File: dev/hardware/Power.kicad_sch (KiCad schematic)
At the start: 5 parts, among them U2 LD1117V33

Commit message: Continued developing JCAP schematic
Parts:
- D301: value LED -> POWER LED
- R301: value R -> 100
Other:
- moved on the sheet: C2, D301, R301, U2

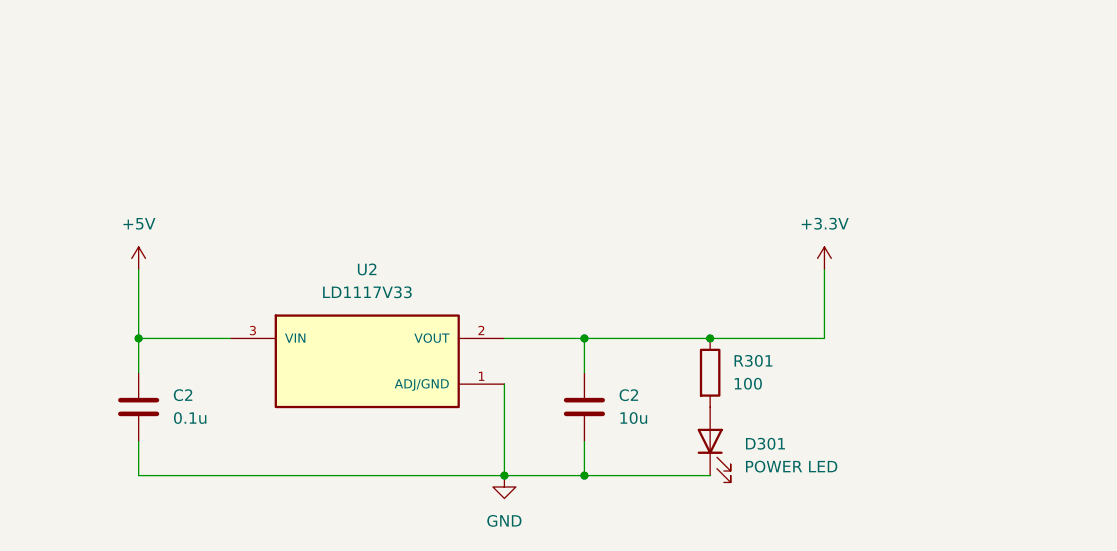
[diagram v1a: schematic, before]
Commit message: Finalized initial schematic
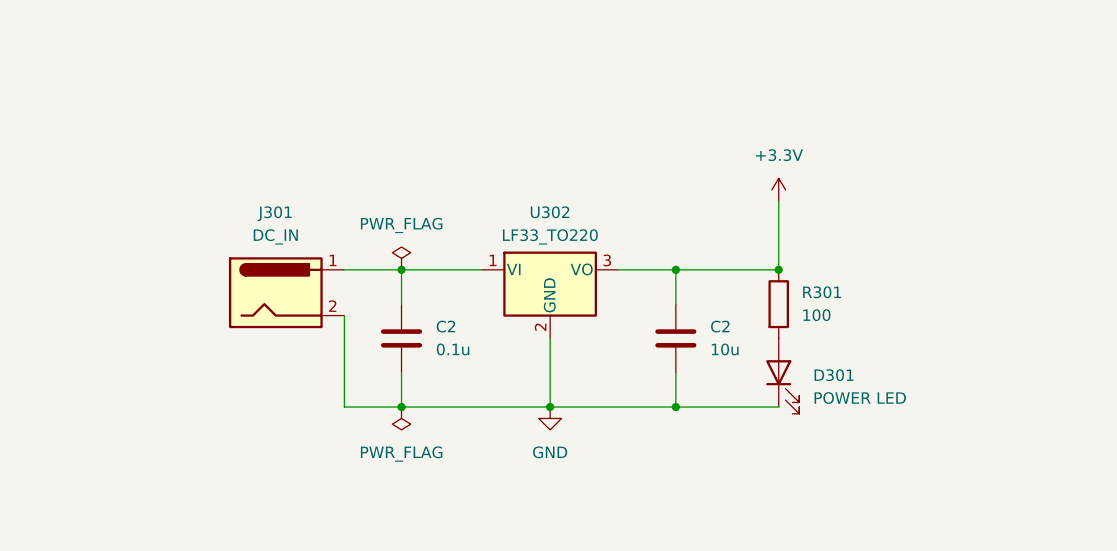
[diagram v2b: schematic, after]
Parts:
- removed U2: LD1117V33, jcap_footprint_library:TO255P1020X450X1968-3, symbol jcap_symbol_library:LD1117V33
- added J301: DC_IN, Connector_BarrelJack:BarrelJack_CUI_PJ-063AH_Horizontal_CircularHoles, symbol Connector:Barrel_Jack
- added U302: LF33_TO220, Package_TO_SOT_THT:TO-220-3_Vertical, symbol Regulator_Linear:LF33_TO220
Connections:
- net +3.3V: now also U302.3 (VO)
- net GND: now also J301.2, U302.2 (GND)
- net +5V: no longer names the net of C2.1
- net +5V: now also J301.1, U302.1 (VI)
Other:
- moved on the sheet: C2, D301, R301

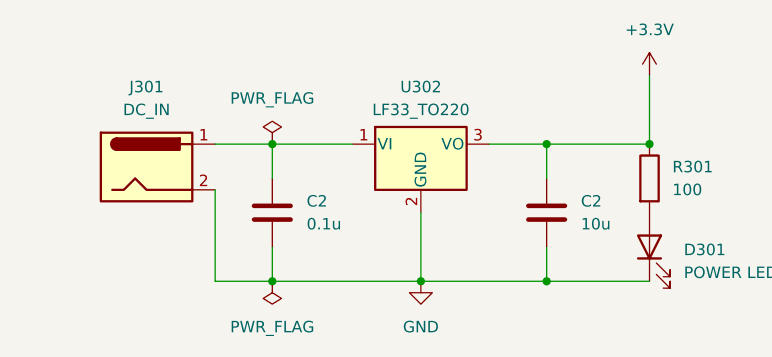
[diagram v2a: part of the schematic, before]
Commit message: Started developing PCB layout
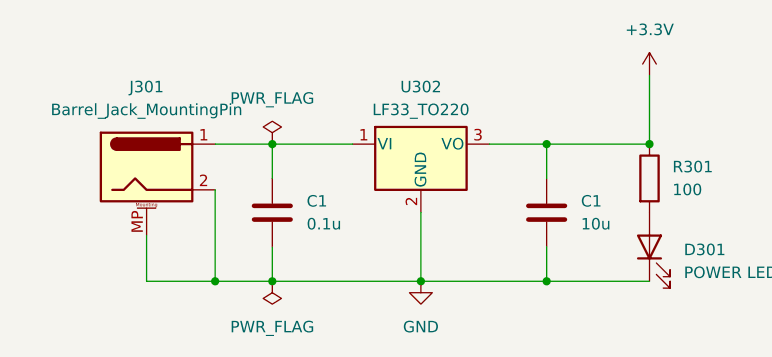
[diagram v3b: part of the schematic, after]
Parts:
- removed C2: 10u, Capacitor_THT:C_Radial_D4.0mm_H7.0mm_P1.50mm, symbol Device:C
- removed C2: 0.1u, Capacitor_THT:C_Radial_D4.0mm_H7.0mm_P1.50mm, symbol Device:C
- removed J301: DC_IN, Connector_BarrelJack:BarrelJack_CUI_PJ-063AH_Horizontal_CircularHoles, symbol Connector:Barrel_Jack
- added C1: 0.1u, Capacitor_THT:C_Disc_D3.4mm_W2.1mm_P2.50mm, symbol Device:C
- added C1: 10u, Capacitor_THT:C_Disc_D3.4mm_W2.1mm_P2.50mm, symbol Device:C
- added J301: Barrel_Jack_MountingPin, Connector_BarrelJack:BarrelJack_CUI_PJ-063AH_Horizontal_CircularHoles, symbol Connector:Barrel_Jack_MountingPin
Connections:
- net +3.3V: now also C1.2
- net GND: now also C1.1, C1.1, J301.2, J301.MP (MountPin)
- net at U302.1 (VI): now also C1.2, J301.1
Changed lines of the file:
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@@
   (junction (at 130.81 102.87) (diameter 0) (color 0 0 0 0)
   )
+  (junction (at 124.46 102.87) (diameter 0) (color 0 0 0 0)
+  )
   (junction (at 147.32 102.87) (diameter 0) (color 0 0 0 0)
   )
@@
     (stroke (width 0) (type default))
   )
+  (wire (pts (xy 116.84 97.79) (xy 116.84 102.87))
+    (stroke (width 0) (type default))
+  )
   (wire (pts (xy 147.32 95.25) (xy 147.32 102.87))
     (stroke (width 0) (type default))
@@
     (stroke (width 0) (type default))
   )
+  (wire (pts (xy 116.84 102.87) (xy 124.46 102.87))
+    (stroke (width 0) (type default))
+  )
   (wire (pts (xy 130.81 99.06) (xy 130.81 102.87))
     (stroke (width 0) (type default))
   )
+  (symbol (lib_id "Connector:Barrel_Jack_MountingPin") (at 116.84 90.17 0) (unit 1)
+    (in_bom yes) (on_board yes) (dnp no) (fields_autoplaced)
+    (property "Reference" "J301" (at 116.84 81.28 0)
+      (effects (font (size 1.27 1.27)))
+    )
+    (property "Value" "Barrel_Jack_MountingPin" (at 116.84 83.82 0)
+      (effects (font (size 1.27 1.27)))
+    )
+    (property "Footprint" "Connector_BarrelJack:BarrelJack_CUI_PJ-063AH_Horizontal_CircularHoles" (at 118.11 91.186 0)
+      (effects (font (size 1.27 1.27)) hide)
+    )
+    (property "Datasheet" "~" (at 118.11 91.186 0)
+      (effects (font (size 1.27 1.27)) hide)
+    )
+    (pin "1")
+    (pin "2")
+    (pin "MP")
+    (instances
+      (project "jcap"
+        (path "/7fc25e9e-3600-419b-89ef-b962e4e374c1/f5a50cf1-3d87-469f-beb1-b0b9cfae00ce"
+          (reference "J301") (unit 1)
+        )
+      )
+    )
+  )
   (symbol (lib_id "power:PWR_FLAG") (at 130.81 87.63 0) (unit 1)
     (in_bom yes) (on_board yes) (dnp no) (fields_autoplaced)
@@
         (path "/7fc25e9e-3600-419b-89ef-b962e4e374c1/f5a50cf1-3d87-469f-beb1-b0b9cfae00ce"
           (reference "#FLG0301") (unit 1)
+        )
+      )
+    )
+  )
+  (symbol (lib_id "Device:C") (at 130.81 95.25 180) (unit 1)
+    (in_bom yes) (on_board yes) (dnp no) (fields_autoplaced)
+    (property "Reference" "C1" (at 134.62 93.98 0)
+      (effects (font (size 1.27 1.27)) (justify right))
+    )
+    (property "Value" "0.1u" (at 134.62 96.52 0)
+      (effects (font (size 1.27 1.27)) (justify right))
+    )
+    (property "Footprint" "Capacitor_THT:C_Disc_D3.4mm_W2.1mm_P2.50mm" (at 129.8448 91.44 0)
+      (effects (font (size 1.27 1.27)) hide)
+    )
+    (property "Datasheet" "~" (at 130.81 95.25 0)
+      (effects (font (size 1.27 1.27)) hide)
+    )
+    (pin "1")
+    (pin "2")
+    (instances
+      (project "jcap"
+        (path "/7fc25e9e-3600-419b-89ef-b962e4e374c1"
+          (reference "C1") (unit 1)
+        )
+        (path "/7fc25e9e-3600-419b-89ef-b962e4e374c1/203ea849-2dbb-4e64-89c6-7fa05a05e11f"
+          (reference "C1") (unit 1)
+        )
+        (path "/7fc25e9e-3600-419b-89ef-b962e4e374c1/f5a50cf1-3d87-469f-beb1-b0b9cfae00ce"
+          (reference "C301") (unit 1)
         )
       )
@@
     )
   )
-  (symbol (lib_id "Device:C") (at 161.29 95.25 0) (unit 1)
-    (in_bom yes) (on_board yes) (dnp no) (fields_autoplaced)
-    (property "Reference" "C2" (at 165.1 93.98 0)
-      (effects (font (size 1.27 1.27)) (justify left))
-    )
-    (property "Value" "10u" (at 165.1 96.52 0)
-      (effects (font (size 1.27 1.27)) (justify left))
-    )
-    (property "Footprint" "Capacitor_THT:C_Radial_D4.0mm_H7.0mm_P1.50mm" (at 162.2552 99.06 0)
-      (effects (font (size 1.27 1.27)) hide)
-    )
-    (property "Datasheet" "~" (at 161.29 95.25 0)
-      (effects (font (size 1.27 1.27)) hide)
-    )
-    (pin "1")
-    (pin "2")
-    (instances
-      (project "jcap"
-        (path "/7fc25e9e-3600-419b-89ef-b962e4e374c1"
-          (reference "C2") (unit 1)
-        )
-        (path "/7fc25e9e-3600-419b-89ef-b962e4e374c1/203ea849-2dbb-4e64-89c6-7fa05a05e11f"
-          (reference "C2") (unit 1)
-        )
-        (path "/7fc25e9e-3600-419b-89ef-b962e4e374c1/f5a50cf1-3d87-469f-beb1-b0b9cfae00ce"
-          (reference "C302") (unit 1)
-        )
-      )
-    )
-  )
-  (symbol (lib_id "Connector:Barrel_Jack") (at 116.84 90.17 0) (unit 1)
-    (in_bom yes) (on_board yes) (dnp no) (fields_autoplaced)
-    (property "Reference" "J301" (at 116.84 81.28 0)
-      (effects (font (size 1.27 1.27)))
-    )
-    (property "Value" "DC_IN" (at 116.84 83.82 0)
-      (effects (font (size 1.27 1.27)))
-    )
-    (property "Footprint" "Connector_BarrelJack:BarrelJack_CUI_PJ-063AH_Horizontal_CircularHoles" (at 118.11 91.186 0)
-      (effects (font (size 1.27 1.27)) hide)
-    )
-    (property "Datasheet" "~" (at 118.11 91.186 0)
-      (effects (font (size 1.27 1.27)) hide)
-    )
-    (pin "1")
-    (pin "2")
-    (instances
-      (project "jcap"
-        (path "/7fc25e9e-3600-419b-89ef-b962e4e374c1/f5a50cf1-3d87-469f-beb1-b0b9cfae00ce"
-          (reference "J301") (unit 1)
-        )
-      )
-    )
-  )
-  (symbol (lib_id "Device:C") (at 130.81 95.25 0) (unit 1)
-    (in_bom yes) (on_board yes) (dnp no) (fields_autoplaced)
-    (property "Reference" "C2" (at 134.62 93.98 0)
-      (effects (font (size 1.27 1.27)) (justify left))
-    )
-    (property "Value" "0.1u" (at 134.62 96.52 0)
-      (effects (font (size 1.27 1.27)) (justify left))
-    )
-    (property "Footprint" "Capacitor_THT:C_Radial_D4.0mm_H7.0mm_P1.50mm" (at 131.7752 99.06 0)
-      (effects (font (size 1.27 1.27)) hide)
-    )
-    (property "Datasheet" "~" (at 130.81 95.25 0)
-      (effects (font (size 1.27 1.27)) hide)
-    )
-    (pin "1")
-    (pin "2")
-    (instances
-      (project "jcap"
-        (path "/7fc25e9e-3600-419b-89ef-b962e4e374c1"
-          (reference "C2") (unit 1)
-        )
-        (path "/7fc25e9e-3600-419b-89ef-b962e4e374c1/203ea849-2dbb-4e64-89c6-7fa05a05e11f"
-          (reference "C2") (unit 1)
-        )
-        (path "/7fc25e9e-3600-419b-89ef-b962e4e374c1/f5a50cf1-3d87-469f-beb1-b0b9cfae00ce"
-          (reference "C301") (unit 1)
-        )
-      )
-    )
-  )
   (symbol (lib_id "power:PWR_FLAG") (at 130.81 102.87 180) (unit 1)
     (in_bom yes) (on_board yes) (dnp no) (fields_autoplaced)
@@
         )
       )
+    )
+  )
+  (symbol (lib_id "Device:C") (at 161.29 95.25 180) (unit 1)
+    (in_bom yes) (on_board yes) (dnp no) (fields_autoplaced)
+    (property "Reference" "C1" (at 165.1 93.98 0)
+      (effects (font (size 1.27 1.27)) (justify right))
+    )
+    (property "Value" "10u" (at 165.1 96.52 0)
+      (effects (font (size 1.27 1.27)) (justify right))
+    )
+    (property "Footprint" "Capacitor_THT:C_Disc_D3.4mm_W2.1mm_P2.50mm" (at 160.3248 91.44 0)
+      (effects (font (size 1.27 1.27)) hide)
+    )
+    (property "Datasheet" "~" (at 161.29 95.25 0)
+      (effects (font (size 1.27 1.27)) hide)
+    )
+    (pin "1")
+    (pin "2")
+    (instances
+      (project "jcap"
+        (path "/7fc25e9e-3600-419b-89ef-b962e4e374c1"
+          (reference "C1") (unit 1)
+        )
+        (path "/7fc25e9e-3600-419b-89ef-b962e4e374c1/203ea849-2dbb-4e64-89c6-7fa05a05e11f"
+          (reference "C1") (unit 1)
+        )
+        (path "/7fc25e9e-3600-419b-89ef-b962e4e374c1/f5a50cf1-3d87-469f-beb1-b0b9cfae00ce"
+          (reference "C302") (unit 1)
+        )
+      )

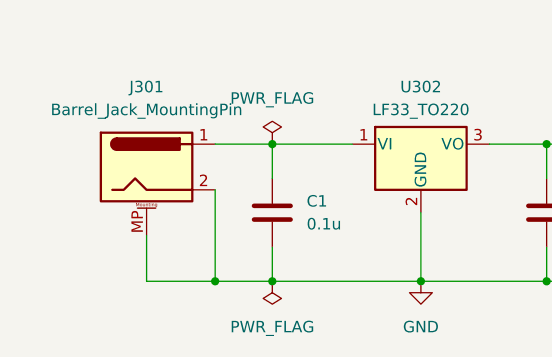
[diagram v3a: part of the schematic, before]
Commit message: Updated netclasses and PCB specs
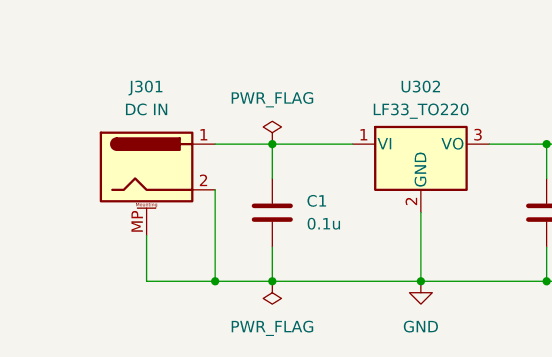
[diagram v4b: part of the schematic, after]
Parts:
- J301: value Barrel_Jack_MountingPin -> DC IN
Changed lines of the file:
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@@
     (stroke (width 0) (type default))
+  )
+  (netclass_flag "" (length 1) (shape dot) (at 172.72 95.25 270) (fields_autoplaced)
+    (effects (font (size 1.27 1.27) (color 255 0 0 1)) (justify right bottom))
+    (property "Netclass" "Power" (at 173.72 94.5515 90)
+      (effects (font (size 1.27 1.27) italic) (justify left) hide)
+    )
+  )
+  (netclass_flag "" (length 1) (shape dot) (at 135.89 87.63 0) (fields_autoplaced)
+    (effects (font (size 1.27 1.27) (color 255 0 0 1)) (justify left bottom))
+    (property "Netclass" "Power" (at 136.5885 86.63 0)
+      (effects (font (size 1.27 1.27) italic) (justify left) hide)
+    )
   )
   (symbol (lib_id "Connector:Barrel_Jack_MountingPin") (at 116.84 90.17 0) (unit 1)
@@
       (effects (font (size 1.27 1.27)))
     )
-    (property "Value" "Barrel_Jack_MountingPin" (at 116.84 83.82 0)
+    (property "Value" "DC IN" (at 116.84 83.82 0)
       (effects (font (size 1.27 1.27)))
     )

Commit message: Ready for routing
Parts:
- U302: footprint Package_TO_SOT_THT:TO-220-3_Vertical -> Package_TO_SOT_THT:TO-220-3_Horizontal_TabDown
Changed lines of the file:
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@@
       (effects (font (size 1.27 1.27)))
     )
-    (property "Footprint" "Package_TO_SOT_THT:TO-220-3_Vertical" (at 147.32 81.915 0)
+    (property "Footprint" "Package_TO_SOT_THT:TO-220-3_Horizontal_TabDown" (at 147.32 81.915 0)
       (effects (font (size 1.27 1.27) italic) hide)
     )

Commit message: Thicc-traced VGA sig test - REVERT HERE
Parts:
- renumbered C1 to C?, U302 to U301
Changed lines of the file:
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@@
   (symbol (lib_id "Device:C") (at 130.81 95.25 180) (unit 1)
     (in_bom yes) (on_board yes) (dnp no) (fields_autoplaced)
-    (property "Reference" "C1" (at 134.62 93.98 0)
+    (property "Reference" "C?" (at 134.62 93.98 0)
       (effects (font (size 1.27 1.27)) (justify right))
     )
@@
       (project "jcap"
         (path "/7fc25e9e-3600-419b-89ef-b962e4e374c1"
-          (reference "C1") (unit 1)
+          (reference "C?") (unit 1)
         )
         (path "/7fc25e9e-3600-419b-89ef-b962e4e374c1/203ea849-2dbb-4e64-89c6-7fa05a05e11f"
-          (reference "C1") (unit 1)
+          (reference "C?") (unit 1)
         )
         (path "/7fc25e9e-3600-419b-89ef-b962e4e374c1/f5a50cf1-3d87-469f-beb1-b0b9cfae00ce"
@@
   (symbol (lib_id "Regulator_Linear:LF33_TO220") (at 147.32 87.63 0) (unit 1)
     (in_bom yes) (on_board yes) (dnp no) (fields_autoplaced)
-    (property "Reference" "U302" (at 147.32 81.28 0)
+    (property "Reference" "U301" (at 147.32 81.28 0)
       (effects (font (size 1.27 1.27)))
     )
@@
       (project "jcap"
         (path "/7fc25e9e-3600-419b-89ef-b962e4e374c1/f5a50cf1-3d87-469f-beb1-b0b9cfae00ce"
-          (reference "U302") (unit 1)
+          (reference "U301") (unit 1)
         )
       )
@@
   (symbol (lib_id "Device:C") (at 161.29 95.25 180) (unit 1)
     (in_bom yes) (on_board yes) (dnp no) (fields_autoplaced)
-    (property "Reference" "C1" (at 165.1 93.98 0)
+    (property "Reference" "C?" (at 165.1 93.98 0)
       (effects (font (size 1.27 1.27)) (justify right))
     )
@@
       (project "jcap"
         (path "/7fc25e9e-3600-419b-89ef-b962e4e374c1"
-          (reference "C1") (unit 1)
+          (reference "C?") (unit 1)
         )
         (path "/7fc25e9e-3600-419b-89ef-b962e4e374c1/203ea849-2dbb-4e64-89c6-7fa05a05e11f"
-          (reference "C1") (unit 1)
+          (reference "C?") (unit 1)
         )
         (path "/7fc25e9e-3600-419b-89ef-b962e4e374c1/f5a50cf1-3d87-469f-beb1-b0b9cfae00ce"
@@
   (symbol (lib_id "power:+3.3V") (at 172.72 80.01 0) (unit 1)
     (in_bom yes) (on_board yes) (dnp no) (fields_autoplaced)
-    (property "Reference" "#PWR0303" (at 172.72 83.82 0)
+    (property "Reference" "#PWR0302" (at 172.72 83.82 0)
       (effects (font (size 1.27 1.27)) hide)
     )
@@
       (project "jcap"
         (path "/7fc25e9e-3600-419b-89ef-b962e4e374c1/f5a50cf1-3d87-469f-beb1-b0b9cfae00ce"
-          (reference "#PWR0303") (unit 1)
+          (reference "#PWR0302") (unit 1)
         )
       )

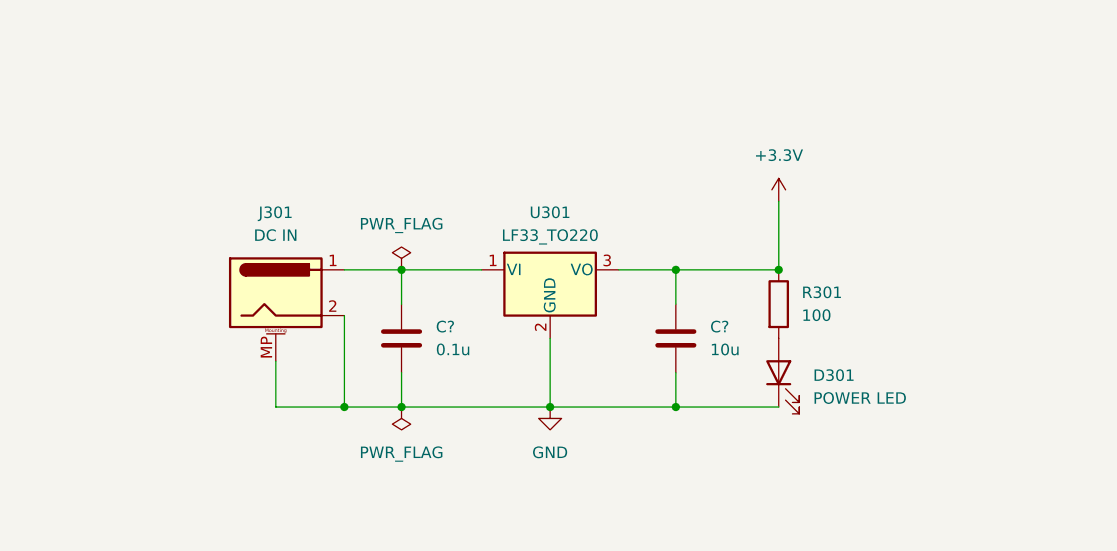
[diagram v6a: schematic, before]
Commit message: Implemented review changes - missing reverse polarity protection
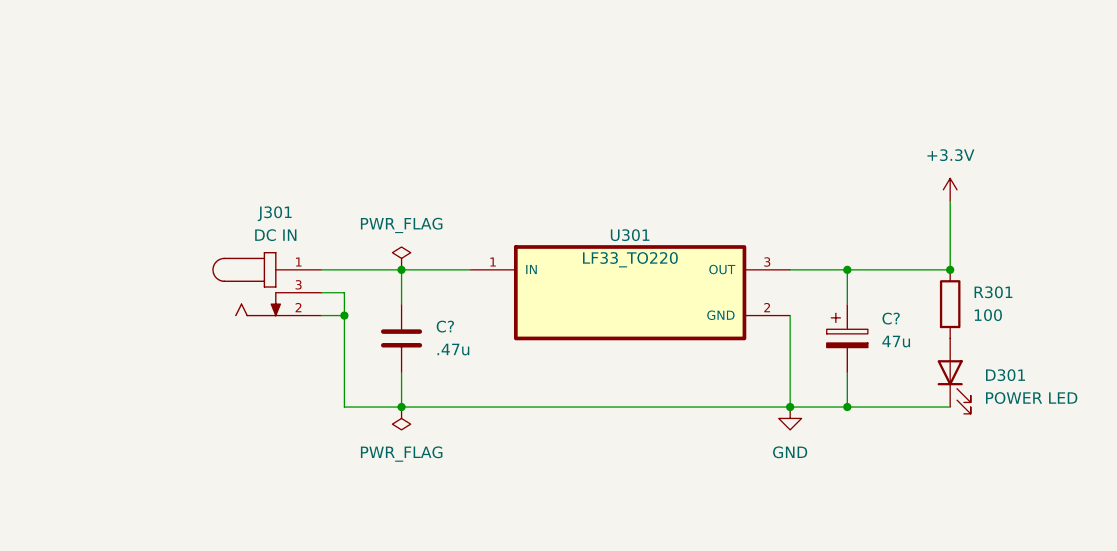
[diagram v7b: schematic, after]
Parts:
- C?: value 0.1u -> .47u
- C?: value 10u -> 47u; footprint Capacitor_THT:C_Disc_D3.4mm_W2.1mm_P2.50mm -> Capacitor_THT:C_Radial_D5.0mm_H11.0mm_P2.00mm; symbol Device:C -> Device:C_Polarized
- J301: footprint Connector_BarrelJack:BarrelJack_CUI_PJ-063AH_Horizontal_CircularHoles -> jcap-footprints:CUI_PJ-202AH; symbol Connector:Barrel_Jack_MountingPin -> jcap-symbols:PJ-202AH
- U301: footprint Package_TO_SOT_THT:TO-220-3_Horizontal_TabDown -> jcap-footprints:TO-220-3_Horizontal_TabDown; symbol Regulator_Linear:LF33_TO220 -> jcap-symbols:LM3940IT-3.3
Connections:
- net +3.3V: now also C?.1; no longer C?.2
- net GND: now also C?.2, J301.3; no longer C?.1, J301.MP (MountPin)
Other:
- moved on the sheet: D301, R301, U301
